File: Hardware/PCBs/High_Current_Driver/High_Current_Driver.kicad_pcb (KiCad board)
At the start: 4 copper layers, 160 x 99.5 mm, 248 parts, among them J1 Conn_01x02, J2 RJ45, J3 Screw_Terminal_01x04, J4 Conn_02x07_Odd_Even, J5 Channel 3, J6 Channel 2, J7 Channel 1, J8 RF_Shield_Two_Pieces, J9 Conn_01x02, Q1 Si4447ADY, Q2 IRF8707PbF, Q3 2SC5566, Q4 2SA2013, Q5 2SC5566, Q6 2SA2013, Q7 2SC5566, Q8 2SA2013, SW1 DPDT_Hirose, U1 LM4040DBZ-5, U10 OPA2210, U11 OPA2210, U12 OPA2210, U13 OPA2210, U14 OPA2210, U2 LM4040DBZ-5, U3 LM393, U4 TPS7A470x, U5 TPS7A470x, U6 TPS7A33, U7 LTC6655-2.5, U8 DAC8814, U9 OPA2210

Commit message: Switch to common footprint library
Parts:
- J1: footprint Dummy_conn_01x02:PinSocket_1x02_P1.00mm_Vertical_CUSTOM_CYD -> vernier_current_driver:PinSocket_1x02_P1.00mm_Vertical_CUSTOM_CYD
- J8: footprint MS570-10F:MS570-10S -> vernier_current_driver:MS570-10S
- R48, R49, R55: footprint WSM2-13R0-FTR-LF:WSM2 13R0 FTR-LF -> vernier_current_driver:WSM2_13R0_FTR-LF
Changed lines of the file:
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@@
       (net 42 /Channel_Outputs/Coil_Iout_R2))
   )
-  (module "WSM2-13R0-FTR-LF:WSM2 13R0 FTR-LF" (layer F.Cu)
+  (module "vernier_current_driver:WSM2_13R0_FTR-LF" (layer F.Cu)
     (at 160.2 118.8 90)
     (fp_text reference R55 (at -3.7 2.15 90) (layer F.SilkS)
@@
       (net 40 /Channel_Outputs/Coil_Iout_R3))
   )
-  (module "WSM2-13R0-FTR-LF:WSM2 13R0 FTR-LF" (layer F.Cu)
+  (module "vernier_current_driver:WSM2_13R0_FTR-LF" (layer F.Cu)
     (at 160.1 92.65 90)
     (fp_text reference R49 (at -3.7 2.15 90) (layer F.SilkS)
@@
       (net 42 /Channel_Outputs/Coil_Iout_R2))
   )
-  (module "WSM2-13R0-FTR-LF:WSM2 13R0 FTR-LF" (layer F.Cu)
+  (module "vernier_current_driver:WSM2_13R0_FTR-LF" (layer F.Cu)
     (at 160.1 66.65 90)
     (fp_text reference R48 (at -3.7 2.15 90) (layer F.SilkS)
@@
       (net 9 GND))
   )
-  (module MS570-10F:MS570-10S (layer F.Cu)
+  (module vernier_current_driver:MS570-10S (layer F.Cu)
     (at 111.2 53.9 90)
     (fp_text reference J8 (at 0.6935 -2.404 180) (layer F.SilkS)
@@
       (net 16 /DAC/Vref_2.5V))
   )
-  (module Dummy_conn_01x02:PinSocket_1x02_P1.00mm_Vertical_CUSTOM_CYD (layer F.Cu)
+  (module vernier_current_driver:PinSocket_1x02_P1.00mm_Vertical_CUSTOM_CYD (layer F.Cu)
     (at 109.0815 85.0125)
     (descr "Through hole straight socket strip, 1x02, 1.00mm pitch, single row (https://gct.co/files/drawings/bc065.pdf), script generated")

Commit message: Bump version to 1.1.0
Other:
- board text added: "HCD v1.1.0 May 2021 Designer: Marcin Mrozowski EQOP"
- board text removed: "HCD Rev 1.0D May 2021 Designer: Marcin Mrozowski EQOP"
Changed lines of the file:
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@@
     (title "\"Vernier Vamp\" Coil Driver - 200mA")
     (date 2020-05-12)
-    (rev 1.0B)
+    (rev 1.1.0)
     (company "Strathclyde University")
     (comment 1 "Designed by: Marcin Mrozowski")
@@
     (effects (font (size 1.5 1.5) (thickness 0.3)))
   )
-  (gr_text "HCD\nRev 1.0D\nMay 2021\nDesigner: Marcin Mrozowski\nEQOP" (at 145.675 132.125) (layer B.SilkS)
+  (gr_text "HCD\nv1.1.0\nMay 2021\nDesigner: Marcin Mrozowski\nEQOP" (at 145.675 132.125) (layer B.SilkS)
     (effects (font (size 1.5 1.5) (thickness 0.3)) (justify mirror))
   )
@@
     (effects (font (size 1.5 1.5) (thickness 0.3)) (justify mirror))
   )
-  (gr_text "HCD\nRev 1.0D\nMay 2021\nDesigner: Marcin Mrozowski\nEQOP" (at 145.625 132.075) (layer F.SilkS)
+  (gr_text "HCD\nv1.1.0\nMay 2021\nDesigner: Marcin Mrozowski\nEQOP" (at 145.625 132.075) (layer F.SilkS)
     (effects (font (size 1.5 1.5) (thickness 0.3)))
   )

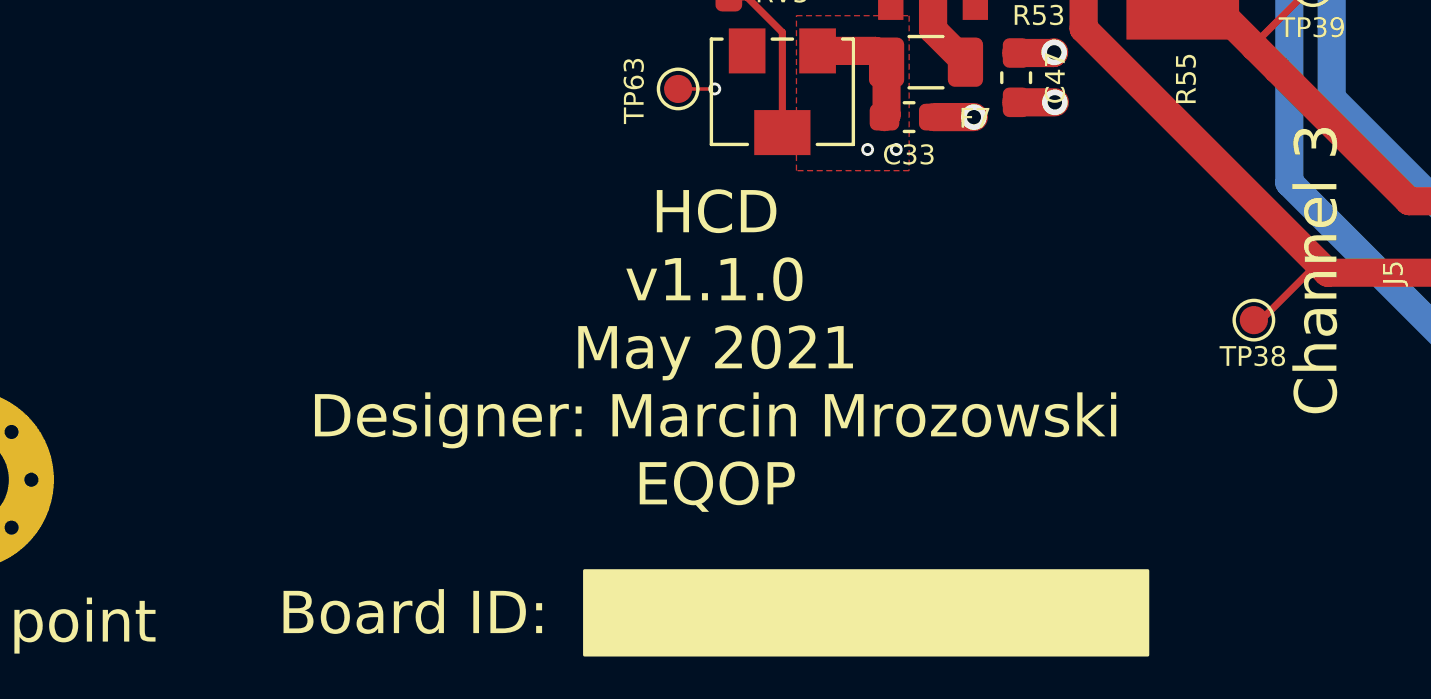
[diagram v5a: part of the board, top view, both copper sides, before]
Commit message: Add repo link to silkscreen
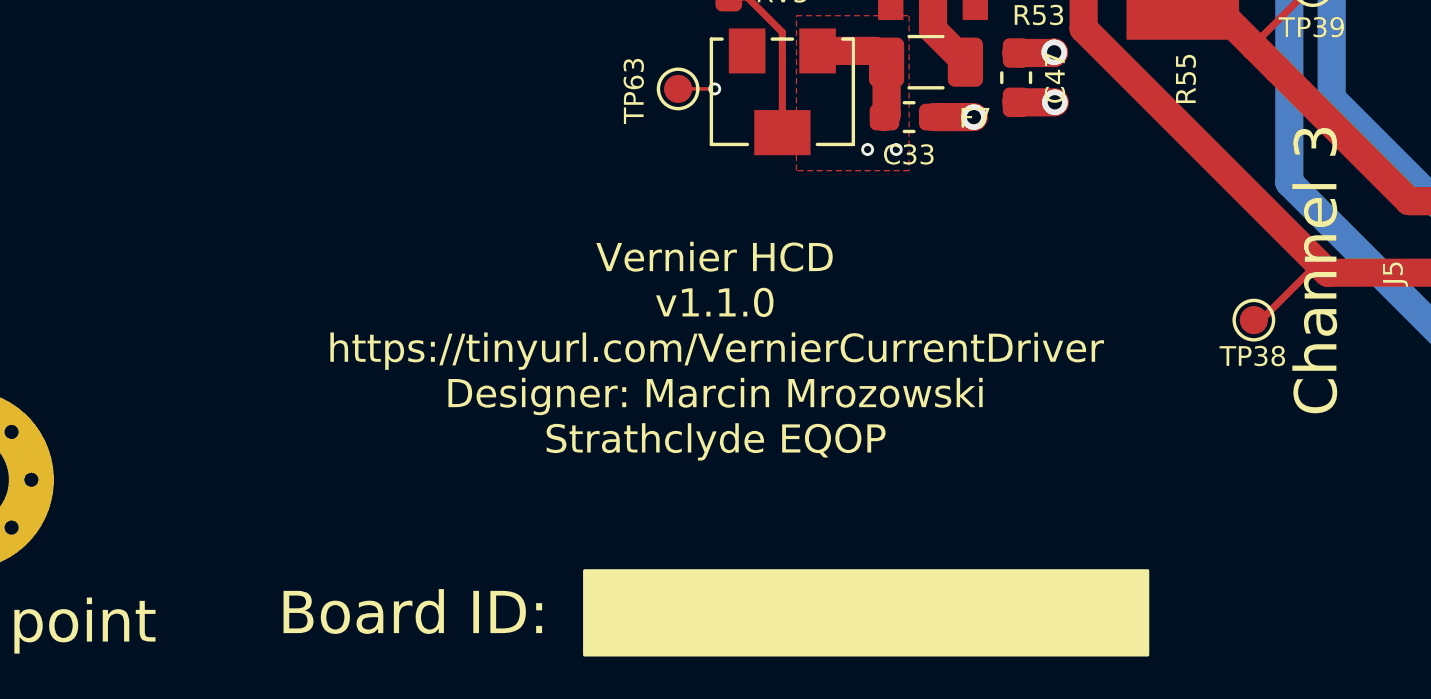
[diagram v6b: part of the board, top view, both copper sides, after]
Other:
- board text added: "Vernier HCD v1.1.0 https://tinyurl.com/VernierCurrentDriver Designer: Marcin Mrozowski Strathclyde EQOP"
- board text removed: "HCD v1.1.0 May 2021 Designer: Marcin Mrozowski EQOP"
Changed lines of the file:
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@@
     (effects (font (size 1.5 1.5) (thickness 0.3)))
   )
-  (gr_text "HCD\nv1.1.0\nMay 2021\nDesigner: Marcin Mrozowski\nEQOP" (at 145.675 132.125) (layer B.SilkS)
-    (effects (font (size 1.5 1.5) (thickness 0.3)) (justify mirror))
+  (gr_text "Vernier HCD\nv1.1.0\nhttps://tinyurl.com/VernierCurrentDriver\nDesigner: Marcin Mrozowski\nStrathclyde EQOP" (at 145.675 132.125) (layer B.SilkS)
+    (effects (font (size 1 1) (thickness 0.15)) (justify mirror))
   )
   (gr_text "Channel 1" (at 166.975 87.775 90) (layer B.SilkS)
@@
     (effects (font (size 1.5 1.5) (thickness 0.3)) (justify mirror))
   )
-  (gr_text "HCD\nv1.1.0\nMay 2021\nDesigner: Marcin Mrozowski\nEQOP" (at 145.625 132.075) (layer F.SilkS)
-    (effects (font (size 1.5 1.5) (thickness 0.3)))
+  (gr_text "Vernier HCD\nv1.1.0\nhttps://tinyurl.com/VernierCurrentDriver\nDesigner: Marcin Mrozowski\nStrathclyde EQOP" (at 145.625 132.075) (layer F.SilkS)
+    (effects (font (size 1 1) (thickness 0.15)))
   )
   (gr_text "Board ID:\n" (at 155.925 141.575) (layer B.SilkS)
